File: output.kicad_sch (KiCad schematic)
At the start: 2 parts

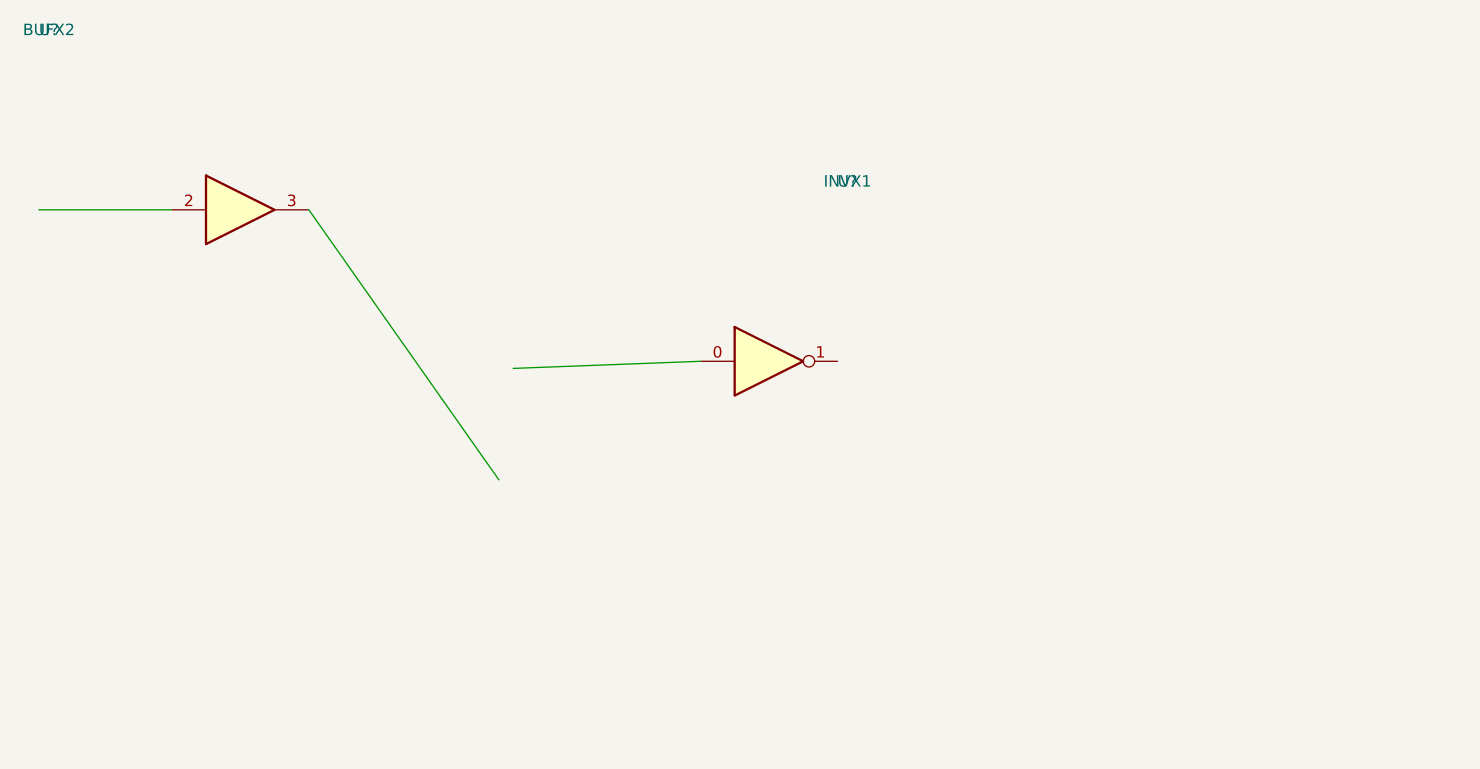
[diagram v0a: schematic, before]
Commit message: improve kicad library handling, improve ltr constraint, detect line crossings
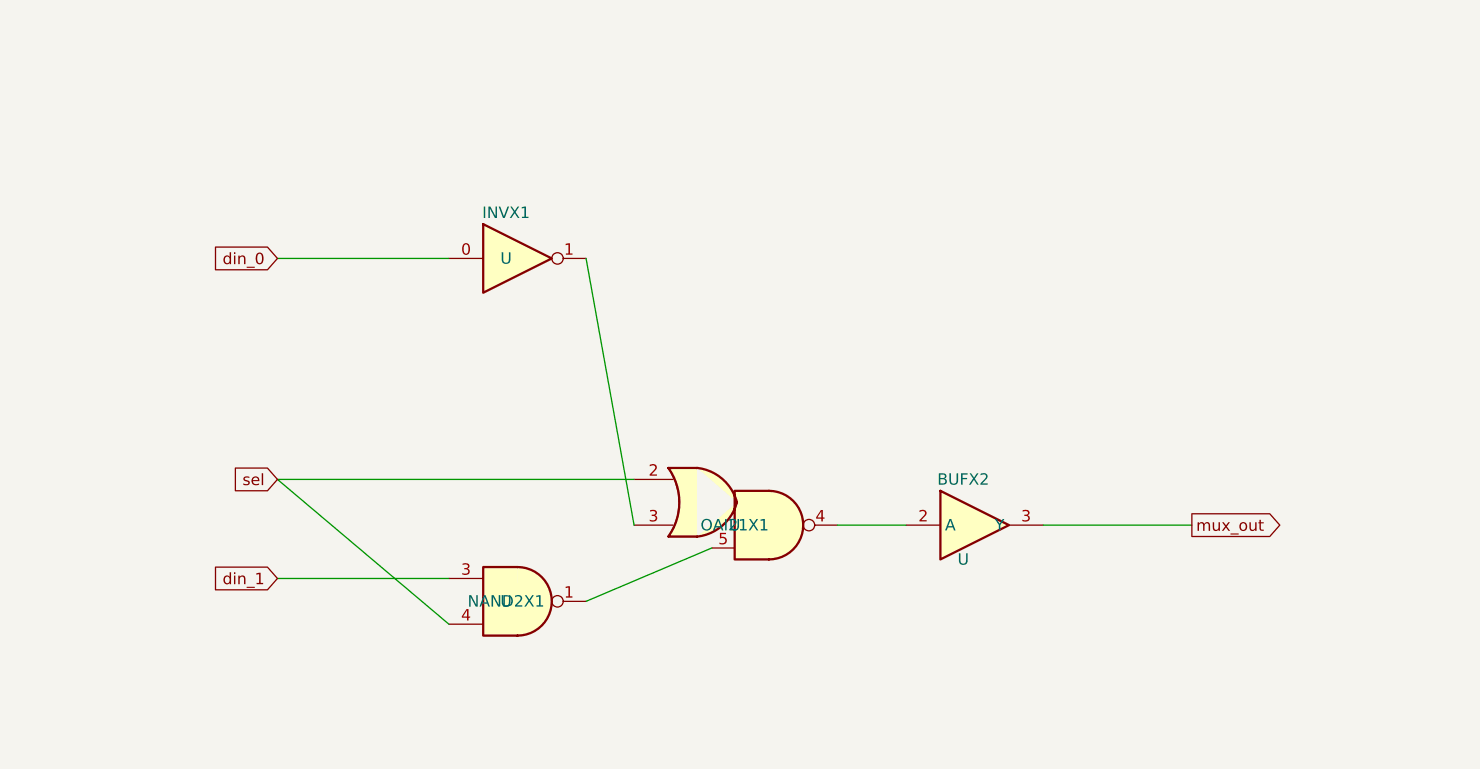
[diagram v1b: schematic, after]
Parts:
- removed U?: INVX1, symbol test:INVX1
- removed U?: BUFX2, symbol test:BUFX2
- added U: NAND2X1, symbol test:NAND2X1
- added U: BUFX2, symbol test:BUFX2
- added U: INVX1, symbol test:INVX1
- added U: OAI21X1, symbol test:OAI21X1
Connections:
- new net: U.1, U.5
- new net: U.2 (A), U.4
- new net: U.1, U.3
- new net din_0: U.0
- new net din_1: U.3
- new net mux_out: U.3 (Y)
- new net sel: U.2, U.4
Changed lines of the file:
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@@
-(kicad_sch (version 20200714) (host eeschema "(5.99.0-2317-g779ed4058)")
-  (page 1 1)
-  (paper "A4")
-  (wire (pts (xy -1.11 20) (xy 13.65 20))
-    (stroke (width 0) (type solid) (color 0 0 0 0))
-  )
-  (wire (pts (xy 28.89 20) (xy 50 50))
-    (stroke (width 0) (type solid) (color 0 0 0 0))
-  )
-  (wire (pts (xy 72.39 36.83) (xy 51.59 37.62))
-    (stroke (width 0) (type solid) (color 0 0 0 0))
-  )
-  (symbol (lib_id "test:BUFX2") (at 20 20 0) (unit 1)
-    (in_bom yes) (on_board yes)
-    (property "Reference" "U?" (id 0) (at 0 0 0))
-    (property "Value" "BUFX2" (id 1) (at 0 0 0))
-    (property "Footprint" "" (id 2) (at 0 0 0)
-      (effects (font (size 1.27 1.27)) hide)
-    )
-    (property "Datasheet" "" (id 3) (at 0 0 0)
-      (effects (font (size 1.27 1.27)) hide)
-    )
-  )
-  (symbol (lib_id "test:INVX1") (at 78.74 36.83 0) (unit 1)
-    (in_bom yes) (on_board yes)
-    (property "Reference" "U?" (id 0) (at 88.74 16.83 0))
-    (property "Value" "INVX1" (id 1) (at 88.74 16.83 0))
-    (property "Footprint" "" (id 2) (at 88.74 16.83 0)
-      (effects (font (size 1.27 1.27)) hide)
-    )
-    (property "Datasheet" "" (id 3) (at 88.74 16.83 0)
-      (effects (font (size 1.27 1.27)) hide)
-    )
-  )
-  (symbol_instances
-    (path "/23d84f5a-cc3f-11ea-a10b-409f38a69f84"
-      (reference "U?") (unit 1)
-    )
-    (path "/23d84f5b-cc3f-11ea-bd56-409f38a69f84"
-      (reference "U?") (unit 1)
-    )
-  )
-)

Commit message: detect component bounding boxes and add constraints for incursions
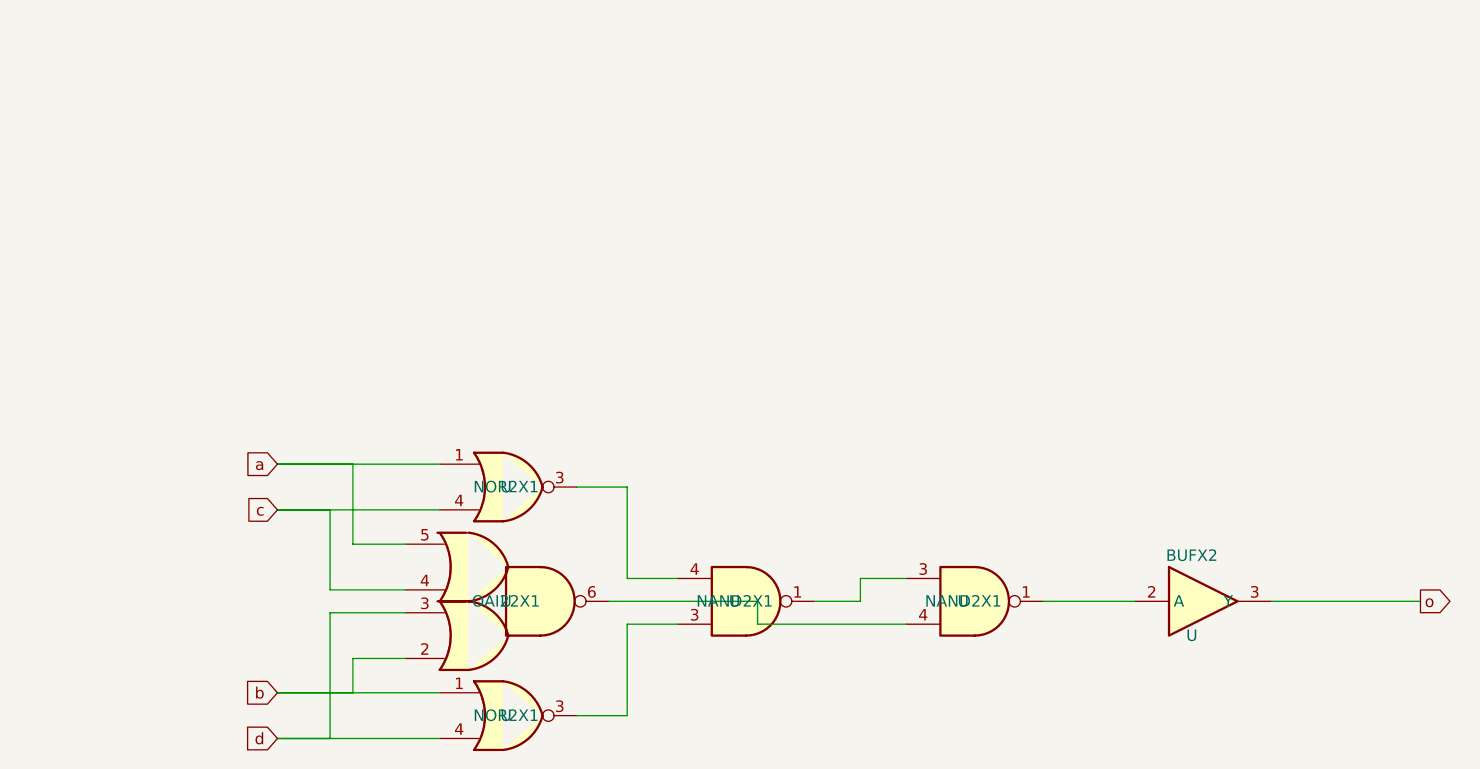
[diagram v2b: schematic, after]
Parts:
- removed U: NAND2X1, symbol test:NAND2X1
- removed U: INVX1, symbol test:INVX1
- removed U: OAI21X1, symbol test:OAI21X1
- added U (x2): NOR2X1, symbol test:NOR2X1
- added U (x2): NAND2X1, symbol test:NAND2X1
- added U: OAI22X1, symbol test:OAI22X1
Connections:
- net at U.2 (A): now also U.1
- net mux_out renamed o
- new net: U.3, U.4
- new net: U.1, U.3
- new net: U.4, U.6
- new net: U.3, U.3
- new net a: U.1, U.5
- new net b: U.1, U.2
- new net c: U.4, U.4
- new net d: U.3, U.4

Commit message: xschem support
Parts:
- removed U (x2): NOR2X1, symbol test:NOR2X1
- removed U (x2): NAND2X1, symbol test:NAND2X1
- added U (x2): NOR2X1, symbol test:NOR2X1
- added U (x2): NAND2X1, symbol test:NAND2X1
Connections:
- net a: now also U.1
- net b: now also U.1
- net c: now also U.4
- net d: now also U.4
- net at U.2 (A): now also U.1
- net at U.6: now also U.4
- new net: U.3, U.4
- new net: U.1, U.3
- new net: U.3, U.3
